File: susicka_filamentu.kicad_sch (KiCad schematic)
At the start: 35 parts, among them J1 USB_C_Receptacle_USB2.0_16P, J2 Conn_01x03, J3 Conn_01x04, J5 Screw_Terminal_01x02, J6 Conn_01x04, J7 Conn_01x04, Q1 Q_NMOS_GSD, U1 RP2350A-QFN60

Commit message: fix(pcb): populate footprints for C1..C24, R1..R14, J1, J3, L1, L2, Y1 across all schematic sheets to eliminate import errors
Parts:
- C10, C11, C12, C13, C14, C15, C16, C17, C3, C4, C5, C6, C7, C8, C9: footprint (none) -> Capacitor_SMD:C_0805_2012Metric
- J1: footprint (none) -> Connector_USB:USB_C_Receptacle_USB2.0_16P
- J3: footprint (none) -> Connector_PinHeader_2.54mm:PinHeader_1x04_P2.54mm_Vertical
- R10, R2, R3, R4, R5, R6, R7, R8, R9: footprint (none) -> Resistor_SMD:R_0805_2012Metric
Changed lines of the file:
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@@
 			)
 		)
-		(property "Footprint" ""
+		(property "Footprint" "Capacitor_SMD:C_0805_2012Metric"
 			(at 31.4452 81.28 0)
 			(effects
@@
 			)
 		)
-		(property "Footprint" ""
+		(property "Footprint" "Connector_USB:USB_C_Receptacle_USB2.0_16P"
 			(at 33.02 40.64 0)
 			(effects
@@
 			)
 		)
-		(property "Footprint" ""
+		(property "Footprint" "Capacitor_SMD:C_0805_2012Metric"
 			(at 267.6652 35.56 0)
 			(effects
@@
 			)
 		)
-		(property "Footprint" ""
+		(property "Footprint" "Capacitor_SMD:C_0805_2012Metric"
 			(at 204.1652 35.56 0)
 			(effects
@@
 			)
 		)
-		(property "Footprint" ""
+		(property "Footprint" "Capacitor_SMD:C_0805_2012Metric"
 			(at 191.4652 35.56 0)
 			(effects
@@
 			)
 		)
-		(property "Footprint" ""
+		(property "Footprint" "Capacitor_SMD:C_0805_2012Metric"
 			(at 158.4452 30.48 0)
 			(effects
@@
 			)
 		)
-		(property "Footprint" ""
+		(property "Footprint" "Capacitor_SMD:C_0805_2012Metric"
 			(at 229.5652 35.56 0)
 			(effects
@@
 			)
 		)
-		(property "Footprint" ""
+		(property "Footprint" "Resistor_SMD:R_0805_2012Metric"
 			(at 19.812 77.47 90)
 			(effects
@@
 			)
 		)
-		(property "Footprint" ""
+		(property "Footprint" "Capacitor_SMD:C_0805_2012Metric"
 			(at 242.2652 35.56 0)
 			(effects
@@
 			)
 		)
-		(property "Footprint" ""
+		(property "Footprint" "Resistor_SMD:R_0805_2012Metric"
 			(at 257.81 67.818 90)
 			(effects
@@
 			)
 		)
-		(property "Footprint" ""
+		(property "Footprint" "Resistor_SMD:R_0805_2012Metric"
 			(at 247.65 65.278 90)
 			(effects
@@
 			)
 		)
-		(property "Footprint" ""
+		(property "Footprint" "Resistor_SMD:R_0805_2012Metric"
 			(at 120.142 114.3 90)
 			(effects
@@
 			)
 		)
-		(property "Footprint" ""
+		(property "Footprint" "Resistor_SMD:R_0805_2012Metric"
 			(at 208.28 52.578 90)
 			(effects
@@
 			)
 		)
-		(property "Footprint" ""
+		(property "Footprint" "Capacitor_SMD:C_0805_2012Metric"
 			(at 115.2652 109.22 0)
 			(effects
@@
 			)
 		)
-		(property "Footprint" ""
+		(property "Footprint" "Resistor_SMD:R_0805_2012Metric"
 			(at 52.07 32.258 90)
 			(effects
@@
 			)
 		)
-		(property "Footprint" ""
+		(property "Footprint" "Capacitor_SMD:C_0805_2012Metric"
 			(at 169.8752 30.48 0)
 			(effects
@@
 			)
 		)
-		(property "Footprint" ""
+		(property "Footprint" "Capacitor_SMD:C_0805_2012Metric"
 			(at 97.4852 49.53 0)
 			(effects
@@
 			)
 		)
-		(property "Footprint" ""
+		(property "Footprint" "Capacitor_SMD:C_0805_2012Metric"
 			(at 130.5052 33.02 0)
 			(effects
@@
 			)
 		)
-		(property "Footprint" ""
+		(property "Footprint" "Resistor_SMD:R_0805_2012Metric"
 			(at 121.92 27.178 90)
 			(effects
@@
 			)
 		)
-		(property "Footprint" ""
+		(property "Footprint" "Capacitor_SMD:C_0805_2012Metric"
 			(at 216.8652 35.56 0)
 			(effects
@@
 			)
 		)
-		(property "Footprint" ""
+		(property "Footprint" "Resistor_SMD:R_0805_2012Metric"
 			(at 52.07 34.798 90)
 			(effects
@@
 			)
 		)
-		(property "Footprint" ""
+		(property "Footprint" "Capacitor_SMD:C_0805_2012Metric"
 			(at 147.0152 30.48 0)
 			(effects
@@
 			)
 		)
-		(property "Footprint" ""
+		(property "Footprint" "Capacitor_SMD:C_0805_2012Metric"
 			(at 254.9652 35.56 0)
 			(effects
@@
 			)
 		)
-		(property "Footprint" ""
+		(property "Footprint" "Capacitor_SMD:C_0805_2012Metric"
 			(at 107.6452 53.34 0)
 			(effects
@@
 			)
 		)
-		(property "Footprint" ""
+		(property "Footprint" "Resistor_SMD:R_0805_2012Metric"
 			(at 208.28 55.118 90)
 			(effects
@@
 			)
 		)
-		(property "Footprint" ""
+		(property "Footprint" "Connector_PinHeader_2.54mm:PinHeader_1x04_P2.54mm_Vertical"
 			(at 90.17 114.3 0)
 			(effects

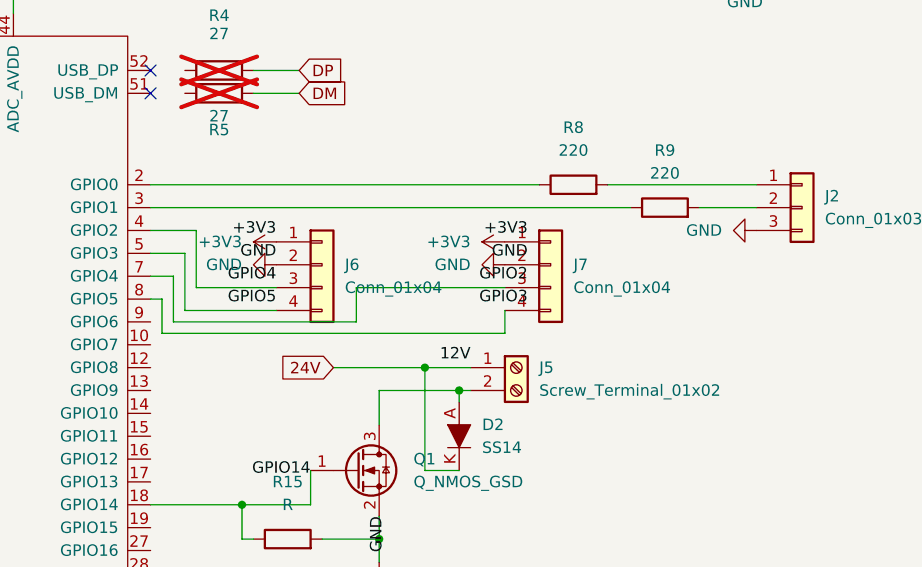
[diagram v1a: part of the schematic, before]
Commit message: feat(pcb): assign exact footprints to all components across all schematic sheets matching BOM soucastky.xlsx
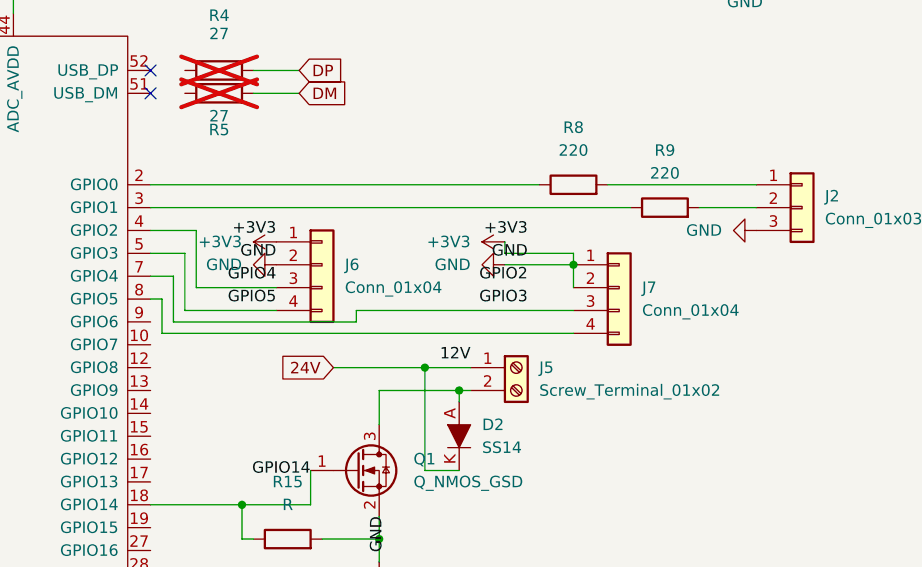
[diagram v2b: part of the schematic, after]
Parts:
- L1: footprint AOTAB201610S3R3101T -> Inductor_SMD:L_0805_2012Metric
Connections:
- net GND is gone; now on net +3V3: C10.2, C11.2, C12.2, C13.2, C14.2, C15.2, C16.2, C17.2, C3.2, C4.2, C5.2, C6.2, C7.1, C8.2, C9.2, J1.A1 (GND), J1.A12 (GND), J1.B1 (GND), J1.B12 (GND), J2.3 (Pin_3), J3.3 (Pin_3), J6.2 (Pin_2), J7.2 (Pin_2), Q1.2 (S), R15.2, R2.2, R3.2, R6.2, U1.47 (VREG_PGND), U1.61 (GND)
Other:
- moved on the sheet: J7
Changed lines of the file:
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@@
 	)
 	(junction
+		(at 247.65 72.39)
+		(diameter 0)
+		(color 0 0 0 0)
+	)
+	(junction
 		(at 222.25 124.46)
 		(diameter 0)
@@
 	(wire
 		(pts
+			(xy 247.65 72.39) (xy 247.65 71.12)
+		)
+		(stroke
+			(width 0)
+			(type default)
+		)
+	)
+	(wire
+		(pts
 			(xy 133.35 78.74) (xy 138.43 78.74)
 		)
@@
 	(wire
 		(pts
+			(xy 240.03 71.12) (xy 240.03 69.85)
+		)
+		(stroke
+			(width 0)
+			(type default)
+		)
+	)
+	(wire
+		(pts
 			(xy 21.59 83.82) (xy 30.48 83.82)
 		)
@@
 	(wire
 		(pts
-			(xy 240.03 80.01) (xy 240.03 77.47)
-		)
-		(stroke
-			(width 0)
-			(type default)
-		)
-	)
-	(wire
-		(pts
 			(xy 172.72 40.64) (xy 175.26 40.64)
 		)
@@
 	(wire
 		(pts
+			(xy 247.65 72.39) (xy 240.03 72.39)
+		)
+		(stroke
+			(width 0)
+			(type default)
+		)
+	)
+	(wire
+		(pts
 			(xy 231.14 95.25) (xy 231.14 83.82)
 		)
@@
 	(wire
 		(pts
+			(xy 247.65 71.12) (xy 240.03 71.12)
+		)
+		(stroke
+			(width 0)
+			(type default)
+		)
+	)
+	(wire
+		(pts
 			(xy 142.24 21.59) (xy 142.24 40.64)
 		)
@@
 	(wire
 		(pts
-			(xy 223.52 74.93) (xy 223.52 78.74)
+			(xy 223.52 77.47) (xy 223.52 78.74)
 		)
 		(stroke
@@
 	(wire
 		(pts
+			(xy 247.65 74.93) (xy 247.65 72.39)
+		)
+		(stroke
+			(width 0)
+			(type default)
+		)
+	)
+	(wire
+		(pts
 			(xy 149.86 40.64) (xy 149.86 44.45)
 		)
@@
 	(wire
 		(pts
-			(xy 201.93 80.01) (xy 240.03 80.01)
+			(xy 201.93 80.01) (xy 247.65 80.01)
 		)
 		(stroke
@@
 	(wire
 		(pts
-			(xy 240.03 74.93) (xy 223.52 74.93)
+			(xy 247.65 77.47) (xy 223.52 77.47)
 		)
 		(stroke
@@
 		)
 	)
+	(label "GPIO4"
+		(at 214.63 73.66 180)
+		(effects
+			(font
+				(size 1.27 1.27)
+			)
+			(justify right)
+		)
+	)
+	(label "GPIO5"
+		(at 214.63 76.2 180)
+		(effects
+			(font
+				(size 1.27 1.27)
+			)
+			(justify right)
+		)
+	)
+	(label "GPIO2"
+		(at 242.57 73.66 180)
+		(effects
+			(font
+				(size 1.27 1.27)
+			)
+			(justify right)
+		)
+	)
+	(label "GPIO3"
+		(at 242.57 76.2 180)
+		(effects
+			(font
+				(size 1.27 1.27)
+			)
+			(justify right)
+		)
+	)
+	(label "GPIO14"
+		(at 218.44 95.25 180)
+		(effects
+			(font
+				(size 1.27 1.27)
+			)
+			(justify right)
+		)
+	)
+	(label "+3V3"
+		(at 214.63 68.58 180)
+		(effects
+			(font
+				(size 1.27 1.27)
+			)
+			(justify right)
+		)
+	)
+	(label "+3V3"
+		(at 242.57 68.58 180)
+		(effects
+			(font
+				(size 1.27 1.27)
+			)
+			(justify right)
+		)
+	)
+	(label "GND"
+		(at 214.63 71.12 180)
+		(effects
+			(font
+				(size 1.27 1.27)
+			)
+			(justify right)
+		)
+	)
+	(label "GND"
+		(at 242.57 71.12 180)
+		(effects
+			(font
+				(size 1.27 1.27)
+			)
+			(justify right)
+		)
+	)
+	(label "GND"
+		(at 226.06 100.33 270)
+		(effects
+			(font
+				(size 1.27 1.27)
+			)
+			(justify right)
+		)
+	)
+	(label "12V"
+		(at 236.22 82.55 180)
+		(effects
+			(font
+				(size 1.27 1.27)
+			)
+			(justify right)
+		)
+	)
 	(global_label "DM"
 		(shape input)
@@
 			)
 		)
-		(property "Footprint" "AOTAB201610S3R3101T"
+		(property "Footprint" "Inductor_SMD:L_0805_2012Metric"
 			(at 19.38 57.15 0)
 			(effects
@@
 	(symbol
 		(lib_id "Connector_Generic:Conn_01x04")
-		(at 245.11 72.39 0)
+		(at 252.73 74.93 0)
 		(unit 1)
 		(exclude_from_sim no)
@@
 		(fields_autoplaced yes)
 		(property "Reference" "J7"
-			(at 247.65 72.3899 0)
+			(at 255.27 74.9299 0)
 			(effects
 				(font
@@
 		)
 		(property "Value" "Conn_01x04"
-			(at 247.65 74.9299 0)
+			(at 255.27 77.4699 0)
 			(effects
 				(font
@@
 		)
 		(property "Footprint" "Connector_PinHeader_2.54mm:PinHeader_1x04_P2.54mm_Vertical"
-			(at 245.11 72.39 0)
+			(at 252.73 74.93 0)
 			(effects
 				(font
@@
 		)
 		(property "Datasheet" "~"
-			(at 245.11 72.39 0)
+			(at 252.73 74.93 0)
 			(effects
 				(font
@@
 		)
 		(property "Description" "Generic connector, single row, 01x04, script generated (kicad-library-utils/schlib/autogen/connector/)"
-			(at 245.11 72.39 0)
+			(at 252.73 74.93 0)
 			(effects
 				(font
@@
 		)
 	)
-	(label "GPIO4"
-		(at 214.63 73.66 180)
-		(fields_autoplaced yes)
-		(effects (font (size 1.27 1.27)) (justify right))
-	)
-	(label "GPIO5"
-		(at 214.63 76.20 180)
-		(fields_autoplaced yes)
-		(effects (font (size 1.27 1.27)) (justify right))
-	)
-	(label "GPIO2"
-		(at 242.57 73.66 180)
-		(fields_autoplaced yes)
-		(effects (font (size 1.27 1.27)) (justify right))
-	)
-	(label "GPIO3"
-		(at 242.57 76.20 180)
-		(fields_autoplaced yes)
-		(effects (font (size 1.27 1.27)) (justify right))
-	)
-	(label "GPIO14"
-		(at 218.44 95.25 180)
-		(fields_autoplaced yes)
-		(effects (font (size 1.27 1.27)) (justify right))
-	)
-	(label "+3V3"
-		(at 214.63 68.58 180)
-		(fields_autoplaced yes)
-		(effects (font (size 1.27 1.27)) (justify right))
-	)
-	(label "+3V3"
-		(at 242.57 68.58 180)
-		(fields_autoplaced yes)
-		(effects (font (size 1.27 1.27)) (justify right))
-	)
-	(label "GND"
-		(at 214.63 71.12 180)
-		(fields_autoplaced yes)
-		(effects (font (size 1.27 1.27)) (justify right))
-	)
-	(label "GND"
-		(at 242.57 71.12 180)
-		(fields_autoplaced yes)
-		(effects (font (size 1.27 1.27)) (justify right))
-	)
-	(label "GND"
-		(at 226.06 100.33 270)
-		(fields_autoplaced yes)
-		(effects (font (size 1.27 1.27)) (justify right))
-	)
-	(label "12V"
-		(at 236.22 82.55 180)
-		(fields_autoplaced yes)
-		(effects (font (size 1.27 1.27)) (justify right))
-	)
-(sheet_instances
+	(sheet_instances
 		(path "/"
 			(page "1")

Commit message: Complete senior 4-layer PCB layout & routing with 0 DRC errors and full keepout enforcement
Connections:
- net +3V3: no longer C10.2, C11.2, C12.2, C13.2, C14.2, C15.2, C16.2, C17.2, C3.2, C4.2, C5.2, C6.2, C7.1, C8.2, C9.2, J1.A1 (GND), J1.A12 (GND), J1.B1 (GND), J1.B12 (GND), J2.3 (Pin_3), J3.3 (Pin_3), J6.2 (Pin_2), J7.1 (Pin_1), J7.2 (Pin_2), Q1.2 (S), R15.2, R2.2, R3.2, R6.2, U1.47 (VREG_PGND), U1.61 (GND)
- new net GND: C10.2, C11.2, C12.2, C13.2, C14.2, C15.2, C16.2, C17.2, C3.2, C4.2, C5.2, C6.2, C7.1, C8.2, C9.2, J1.A1 (GND), J1.A12 (GND), J1.B1 (GND), J1.B12 (GND), J2.3 (Pin_3), J3.3 (Pin_3), J6.2 (Pin_2), J7.1 (Pin_1), Q1.2 (S), R15.2, R2.2, R3.2, R6.2, U1.47 (VREG_PGND), U1.61 (GND)
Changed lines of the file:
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@@
 	)
 	(junction
-		(at 247.65 72.39)
-		(diameter 0)
-		(color 0 0 0 0)
-	)
-	(junction
 		(at 222.25 124.46)
 		(diameter 0)
@@
 	(wire
 		(pts
-			(xy 247.65 72.39) (xy 247.65 71.12)
-		)
-		(stroke
-			(width 0)
-			(type default)
-		)
-	)
-	(wire
-		(pts
 			(xy 133.35 78.74) (xy 138.43 78.74)
 		)
@@
 	(wire
 		(pts
-			(xy 247.65 74.93) (xy 247.65 72.39)
-		)
-		(stroke
-			(width 0)
-			(type default)
-		)
-	)
-	(wire
-		(pts
 			(xy 149.86 40.64) (xy 149.86 44.45)
 		)
@@
 		)
 	)
-	(label "GPIO4"
-		(at 214.63 73.66 180)
-		(effects
-			(font
-				(size 1.27 1.27)
-			)
-			(justify right)
-		)
-	)
-	(label "GPIO5"
-		(at 214.63 76.2 180)
-		(effects
-			(font
-				(size 1.27 1.27)
-			)
-			(justify right)
-		)
-	)
-	(label "GPIO2"
-		(at 242.57 73.66 180)
-		(effects
-			(font
-				(size 1.27 1.27)
-			)
-			(justify right)
-		)
-	)
-	(label "GPIO3"
-		(at 242.57 76.2 180)
-		(effects
-			(font
-				(size 1.27 1.27)
-			)
-			(justify right)
-		)
-	)
-	(label "GPIO14"
-		(at 218.44 95.25 180)
-		(effects
-			(font
-				(size 1.27 1.27)
-			)
-			(justify right)
-		)
-	)
-	(label "+3V3"
-		(at 214.63 68.58 180)
-		(effects
-			(font
-				(size 1.27 1.27)
-			)
-			(justify right)
-		)
-	)
-	(label "+3V3"
-		(at 242.57 68.58 180)
-		(effects
-			(font
-				(size 1.27 1.27)
-			)
-			(justify right)
-		)
-	)
-	(label "GND"
-		(at 214.63 71.12 180)
-		(effects
-			(font
-				(size 1.27 1.27)
-			)
-			(justify right)
-		)
-	)
-	(label "GND"
-		(at 242.57 71.12 180)
-		(effects
-			(font
-				(size 1.27 1.27)
-			)
-			(justify right)
-		)
-	)
-	(label "GND"
-		(at 226.06 100.33 270)
-		(effects
-			(font
-				(size 1.27 1.27)
-			)
-			(justify right)
-		)
-	)
-	(label "12V"
-		(at 236.22 82.55 180)
-		(effects
-			(font
-				(size 1.27 1.27)
-			)
-			(justify right)
-		)
-	)
 	(global_label "DM"
 		(shape input)
@@
 		)
 	)
-	(sheet_instances
+	(label "+3V3"
+		(at 214.63 68.58 180)
+		(fields_autoplaced yes)
+		(effects (font (size 1.27 1.27)) (justify right))
+	)
+	(label "GND"
+		(at 214.63 71.12 180)
+		(fields_autoplaced yes)
+		(effects (font (size 1.27 1.27)) (justify right))
+	)
+	(label "GPIO2"
+		(at 214.63 73.66 180)
+		(fields_autoplaced yes)
+		(effects (font (size 1.27 1.27)) (justify right))
+	)
+	(label "GPIO3"
+		(at 214.63 76.20 180)
+		(fields_autoplaced yes)
+		(effects (font (size 1.27 1.27)) (justify right))
+	)
+	(label "+3V3"
+		(at 250.19 71.12 180)
+		(fields_autoplaced yes)
+		(effects (font (size 1.27 1.27)) (justify right))
+	)
+	(label "GND"
+		(at 250.19 73.66 180)
+		(fields_autoplaced yes)
+		(effects (font (size 1.27 1.27)) (justify right))
+	)
+	(label "GPIO4"
+		(at 250.19 76.20 180)
+		(fields_autoplaced yes)
+		(effects (font (size 1.27 1.27)) (justify right))
+	)
+	(label "GPIO5"
+		(at 250.19 78.74 180)
+		(fields_autoplaced yes)
+		(effects (font (size 1.27 1.27)) (justify right))
+	)
+	(label "GPIO14"
+		(at 218.44 95.25 180)
+		(fields_autoplaced yes)
+		(effects (font (size 1.27 1.27)) (justify right))
+	)
+	(label "GND"
+		(at 226.06 100.33 270)
+		(fields_autoplaced yes)
+		(effects (font (size 1.27 1.27)) (justify right))
+	)
+(sheet_instances
 		(path "/"
 			(page "1")

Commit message: Update passive component footprints to 0603 and sync DRC rules
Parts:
- C10, C11, C12, C13, C14, C15, C16, C17, C3, C4, C5, C6, C7, C8, C9: footprint Capacitor_SMD:C_0805_2012Metric -> Capacitor_SMD:C_0603_1608Metric
- R10, R15, R2, R3, R4, R5, R6, R7, R8, R9: footprint Resistor_SMD:R_0805_2012Metric -> Resistor_SMD:R_0603_1608Metric
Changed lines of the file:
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@@
 			)
 		)
-		(property "Footprint" "Capacitor_SMD:C_0805_2012Metric"
+		(property "Footprint" "Capacitor_SMD:C_0603_1608Metric"
 			(at 31.4452 81.28 0)
 			(effects
@@
 			)
 		)
-		(property "Footprint" "Capacitor_SMD:C_0805_2012Metric"
+		(property "Footprint" "Capacitor_SMD:C_0603_1608Metric"
 			(at 267.6652 35.56 0)
 			(effects
@@
 			)
 		)
-		(property "Footprint" "Capacitor_SMD:C_0805_2012Metric"
+		(property "Footprint" "Capacitor_SMD:C_0603_1608Metric"
 			(at 204.1652 35.56 0)
 			(effects
@@
 			)
 		)
-		(property "Footprint" "Capacitor_SMD:C_0805_2012Metric"
+		(property "Footprint" "Capacitor_SMD:C_0603_1608Metric"
 			(at 191.4652 35.56 0)
 			(effects
@@
 			)
 		)
-		(property "Footprint" "Capacitor_SMD:C_0805_2012Metric"
+		(property "Footprint" "Capacitor_SMD:C_0603_1608Metric"
 			(at 158.4452 30.48 0)
 			(effects
@@
 			)
 		)
-		(property "Footprint" "Capacitor_SMD:C_0805_2012Metric"
+		(property "Footprint" "Capacitor_SMD:C_0603_1608Metric"
 			(at 229.5652 35.56 0)
 			(effects
@@
 			)
 		)
-		(property "Footprint" "Resistor_SMD:R_0805_2012Metric"
+		(property "Footprint" "Resistor_SMD:R_0603_1608Metric"
 			(at 19.812 77.47 90)
 			(effects
@@
 			)
 		)
-		(property "Footprint" "Capacitor_SMD:C_0805_2012Metric"
+		(property "Footprint" "Capacitor_SMD:C_0603_1608Metric"
 			(at 242.2652 35.56 0)
 			(effects
@@
 			)
 		)
-		(property "Footprint" "Resistor_SMD:R_0805_2012Metric"
+		(property "Footprint" "Resistor_SMD:R_0603_1608Metric"
 			(at 257.81 67.818 90)
 			(effects
@@
 			)
 		)
-		(property "Footprint" "Resistor_SMD:R_0805_2012Metric"
+		(property "Footprint" "Resistor_SMD:R_0603_1608Metric"
 			(at 215.9 104.648 90)
 			(effects
@@
 			)
 		)
-		(property "Footprint" "Resistor_SMD:R_0805_2012Metric"
+		(property "Footprint" "Resistor_SMD:R_0603_1608Metric"
 			(at 247.65 65.278 90)
 			(effects
@@
 			)
 		)
-		(property "Footprint" "Resistor_SMD:R_0805_2012Metric"
+		(property "Footprint" "Resistor_SMD:R_0603_1608Metric"
 			(at 120.142 114.3 90)
 			(effects
@@
 			)
 		)
-		(property "Footprint" "Resistor_SMD:R_0805_2012Metric"
+		(property "Footprint" "Resistor_SMD:R_0603_1608Metric"
 			(at 208.28 52.578 90)
 			(effects
@@
 			)
 		)
-		(property "Footprint" "Capacitor_SMD:C_0805_2012Metric"
+		(property "Footprint" "Capacitor_SMD:C_0603_1608Metric"
 			(at 115.2652 109.22 0)
 			(effects
@@
 			)
 		)
-		(property "Footprint" "Resistor_SMD:R_0805_2012Metric"
+		(property "Footprint" "Resistor_SMD:R_0603_1608Metric"
 			(at 52.07 32.258 90)
 			(effects
@@
 			)
 		)
-		(property "Footprint" "Capacitor_SMD:C_0805_2012Metric"
+		(property "Footprint" "Capacitor_SMD:C_0603_1608Metric"
 			(at 169.8752 30.48 0)
 			(effects
@@
 			)
 		)
-		(property "Footprint" "Capacitor_SMD:C_0805_2012Metric"
+		(property "Footprint" "Capacitor_SMD:C_0603_1608Metric"
 			(at 97.4852 49.53 0)
 			(effects
@@
 			)
 		)
-		(property "Footprint" "Capacitor_SMD:C_0805_2012Metric"
+		(property "Footprint" "Capacitor_SMD:C_0603_1608Metric"
 			(at 130.5052 33.02 0)
 			(effects
@@
 			)
 		)
-		(property "Footprint" "Resistor_SMD:R_0805_2012Metric"
+		(property "Footprint" "Resistor_SMD:R_0603_1608Metric"
 			(at 121.92 27.178 90)
 			(effects
@@
 			)
 		)
-		(property "Footprint" "Capacitor_SMD:C_0805_2012Metric"
+		(property "Footprint" "Capacitor_SMD:C_0603_1608Metric"
 			(at 216.8652 35.56 0)
 			(effects
@@
 			)
 		)
-		(property "Footprint" "Resistor_SMD:R_0805_2012Metric"
+		(property "Footprint" "Resistor_SMD:R_0603_1608Metric"
 			(at 52.07 34.798 90)
 			(effects
@@
 			)
 		)
-		(property "Footprint" "Capacitor_SMD:C_0805_2012Metric"
+		(property "Footprint" "Capacitor_SMD:C_0603_1608Metric"
 			(at 147.0152 30.48 0)
 			(effects
@@
 			)
 		)
-		(property "Footprint" "Capacitor_SMD:C_0805_2012Metric"
+		(property "Footprint" "Capacitor_SMD:C_0603_1608Metric"
 			(at 254.9652 35.56 0)
 			(effects
@@
 			)
 		)
-		(property "Footprint" "Capacitor_SMD:C_0805_2012Metric"
+		(property "Footprint" "Capacitor_SMD:C_0603_1608Metric"
 			(at 107.6452 53.34 0)
 			(effects
@@
 			)
 		)
-		(property "Footprint" "Resistor_SMD:R_0805_2012Metric"
+		(property "Footprint" "Resistor_SMD:R_0603_1608Metric"
 			(at 208.28 55.118 90)
 			(effects
